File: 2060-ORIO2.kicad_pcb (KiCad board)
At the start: 4 copper layers, 99 x 99 mm, 159 parts, among them J1 TBL001-500-02GY-2GY, J101 RaspberryPI-B+header, J133 Conn_02x05_Odd_Even, J134 Conn_01x04, J301 Conn_01x08, J302 Conn_01x08, J303 Conn_01x08, J304 Conn_01x08, J305 Conn_01x08, J306 Conn_01x08, J307 Conn_01x08, J308 Conn_01x08, J321 Conn_01x08, J322 Conn_01x08, J323 Conn_01x08, J331 Conn_01x08, J332 Conn_01x08, J333 Conn_01x08, J341 Conn_01x10, J342 Conn_01x10, J343 Conn_01x10, J35 Conn_01x02, J351 Conn_01x10, J352 Conn_01x10, J353 Conn_01x10, J354 Conn_01x10, Q101 DMG2305UX-13, Q102 ULN2803ADWR, Q103 DMMT5401, SW101 SW_DIP_x08, U1 TPS563231, U10 SN74LVC4245AN, U102 AZ1117CH-3.3TRG1, U103 AZ1117CH-1.2, U104 ICE40HX4K-TQ144, U105 MCP3008, U11 AZ1117CH-3.3TRG1, U12 AP3012, U2 TPS563231, U3 SN74LVC4245AN, U4 SN74LVC4245AN, U5 SN74LVC4245AN, U6 SN74LVC4245AN, U7 SN74LVC4245AN, U8 TPS563231, U9 SN74LVC4245AN, Y101 XLH536025_000000I

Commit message: checkpoint
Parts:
- removed J133: Conn_02x05_Odd_Even, Connector_PinHeader_2.54mm:PinHeader_2x05_P2.54mm_Vertical
- removed Q101: DMG2305UX-13, digikey-footprints:SOT-23-3
- removed Q103: DMMT5401, Package_TO_SOT_SMD:SOT-23-6
- removed R101, R102: 22, Resistor_SMD:R_0603_1608Metric_Pad1.05x0.95mm_HandSolder
- removed RN102, RN103: R_Pack08, Resistor_SMD:R_Array_Convex_8x0602
- added C3: X, Capacitor_SMD:C_0603_1608Metric_Pad1.05x0.95mm_HandSolder, F.Cu at (127.1, 126.5)
- added C39: X, Capacitor_SMD:C_0603_1608Metric_Pad1.05x0.95mm_HandSolder, F.Cu at (129.6, 126.5)
- added C40: X, Capacitor_SMD:C_0603_1608Metric_Pad1.05x0.95mm_HandSolder, F.Cu at (132.2, 126.5)
- added C41: X, Capacitor_SMD:C_0603_1608Metric_Pad1.05x0.95mm_HandSolder, F.Cu at (134.7, 126.5)
- added C42: X, Capacitor_SMD:C_0603_1608Metric_Pad1.05x0.95mm_HandSolder, F.Cu at (137.2, 126.5)
- added C43: X, Capacitor_SMD:C_0603_1608Metric_Pad1.05x0.95mm_HandSolder, F.Cu at (139.8, 126.5)
- added C44: X, Capacitor_SMD:C_0603_1608Metric_Pad1.05x0.95mm_HandSolder, F.Cu at (142.3, 126.5)
- added C45: X, Capacitor_SMD:C_0603_1608Metric_Pad1.05x0.95mm_HandSolder, F.Cu at (144.9, 126.5)
- added R10: X, Resistor_SMD:R_0603_1608Metric_Pad1.05x0.95mm_HandSolder, F.Cu at (115.3, 51.3)
- added R11: X, Resistor_SMD:R_0603_1608Metric_Pad1.05x0.95mm_HandSolder, F.Cu at (118.4, 51.3)
- added R12: X, Resistor_SMD:R_0603_1608Metric_Pad1.05x0.95mm_HandSolder, F.Cu at (125.0, 62.3)
- added R13: X, Resistor_SMD:R_0603_1608Metric_Pad1.05x0.95mm_HandSolder, F.Cu at (116.8, 51.3)
- added R14: X, Resistor_SMD:R_0603_1608Metric_Pad1.05x0.95mm_HandSolder, F.Cu at (110.6, 51.3)
- added R15: X, Resistor_SMD:R_0603_1608Metric_Pad1.05x0.95mm_HandSolder, F.Cu at (113.6, 51.3)
- added R16: X, Resistor_SMD:R_0603_1608Metric_Pad1.05x0.95mm_HandSolder, F.Cu at (127.1, 129.9)
- added R17: X, Resistor_SMD:R_0603_1608Metric_Pad1.05x0.95mm_HandSolder, F.Cu at (129.6, 129.9)
- added R18: X, Resistor_SMD:R_0603_1608Metric_Pad1.05x0.95mm_HandSolder, F.Cu at (132.2, 129.9)
- added R19: X, Resistor_SMD:R_0603_1608Metric_Pad1.05x0.95mm_HandSolder, F.Cu at (134.7, 129.9)
- added R20: X, Resistor_SMD:R_0603_1608Metric_Pad1.05x0.95mm_HandSolder, F.Cu at (137.2, 129.9)
- added R21: X, Resistor_SMD:R_0603_1608Metric_Pad1.05x0.95mm_HandSolder, F.Cu at (139.8, 129.9)
- added R22: X, Resistor_SMD:R_0603_1608Metric_Pad1.05x0.95mm_HandSolder, F.Cu at (142.3, 129.9)
- added R23: X, Resistor_SMD:R_0603_1608Metric_Pad1.05x0.95mm_HandSolder, F.Cu at (144.9, 129.9)
- added R24: X, Resistor_SMD:R_0603_1608Metric_Pad1.05x0.95mm_HandSolder, F.Cu at (127.1, 123.2)
- added R25: X, Resistor_SMD:R_0603_1608Metric_Pad1.05x0.95mm_HandSolder, F.Cu at (129.6, 123.2)
- added R26: X, Resistor_SMD:R_0603_1608Metric_Pad1.05x0.95mm_HandSolder, F.Cu at (132.2, 123.2)
- added R27: X, Resistor_SMD:R_0603_1608Metric_Pad1.05x0.95mm_HandSolder, F.Cu at (134.7, 123.2)
- added R28: X, Resistor_SMD:R_0603_1608Metric_Pad1.05x0.95mm_HandSolder, F.Cu at (137.2, 123.2)
- added R29: X, Resistor_SMD:R_0603_1608Metric_Pad1.05x0.95mm_HandSolder, F.Cu at (139.8, 123.2)
- added R30: X, Resistor_SMD:R_0603_1608Metric_Pad1.05x0.95mm_HandSolder, F.Cu at (142.3, 123.2)
- added R31: X, Resistor_SMD:R_0603_1608Metric_Pad1.05x0.95mm_HandSolder, F.Cu at (144.9, 123.2)
- added R9: X, Resistor_SMD:R_0603_1608Metric_Pad1.05x0.95mm_HandSolder, F.Cu at (112.1, 51.3)
- J321: value Conn_01x08 -> Conn_01x09; footprint Connector_PinHeader_2.54mm:PinHeader_1x08_P2.54mm_Vertical -> Connector_PinHeader_2.54mm:PinHeader_1x09_P2.54mm_Vertical
- J341, J342, J343: value Conn_01x10 -> Conn_01x16; footprint Connector_PinHeader_2.54mm:PinHeader_1x10_P2.54mm_Vertical -> Connector_PinHeader_2.54mm:PinHeader_1x16_P2.54mm_Vertical
- U12: footprint Package_TO_SOT_SMD:SOT-23-5_HandSoldering -> Package_TO_SOT_SMD:SOT-23-5
- moved C120 47.4 mm to (142.9, 60.5), turned to 90 degrees
- moved RN101 45.0 mm to (121.7, 51.7)
- moved D0 44.6 mm to (120.9, 56.0), turned to 270 degrees
- moved D1 43.7 mm to (122.9, 56.0), turned to 270 degrees
- moved D2 43.0 mm to (124.9, 56.0), turned to 270 degrees
- moved D3 42.5 mm to (127.0, 56.0), turned to 270 degrees
- moved D7 42.4 mm to (135.1, 56.0), turned to 270 degrees
- moved D4 42.2 mm to (129.0, 56.0), turned to 270 degrees
- moved D6 42.2 mm to (133.1, 56.0), turned to 270 degrees
- moved D5 42.1 mm to (131.0, 56.0), turned to 270 degrees
- moved C119 37.0 mm to (123.4, 66.3)
- moved C111 34.1 mm to (119.8, 85.7), turned to 180 degrees
- moved SW101 28.1 mm to (104.1, 98.5), turned to 180 degrees
- moved R5 26.1 mm to (114.9, 107.2), turned to 0 degrees
- moved C29 25.6 mm to (109.5, 115.0), turned to 270 degrees
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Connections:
- net /IOT_197 renamed Net-(U104-Pad128)
- net Net-(J301-Pad6) renamed /FIO10
- net Net-(J303-Pad3) renamed /FIO5
- C22 pad 1: VCC_IO -> +3V3
- J101 pad 16: /CDONE -> /GPIO23
- J101 pad 18: /~CRESET~ -> /GPIO24
- J101 pad 19: /FPGA_MOSI -> /SPI_MOSI
- J101 pad 21: /FPGA_MISO -> /SPI_MISO
- J101 pad 23: /FPGA_SCLK -> /SPI_SCLK
- J101 pad 36: /FPGA_SSEL -> /GPIO16
- J301 pad 1: Net-(J301-Pad1) -> /FIO0
- J301 pad 2: Net-(J301-Pad2) -> /FIO2
- J301 pad 3: Net-(J301-Pad3) -> /FIO4
- J301 pad 4: Net-(J301-Pad4) -> /FIO6
- J301 pad 5: Net-(J301-Pad5) -> /FIO8
- J301 pad 7: Net-(J301-Pad7) -> /FIO12
- J301 pad 8: Net-(J301-Pad8) -> /FIO14
- J303 pad 1: Net-(J303-Pad1) -> /FIO1
- J303 pad 2: Net-(J303-Pad2) -> /FIO3
- J303 pad 4: Net-(J303-Pad4) -> /FIO7
- J303 pad 5: Net-(J303-Pad5) -> /FIO9
- J303 pad 6: Net-(J303-Pad6) -> /FIO11
- J303 pad 7: Net-(J303-Pad7) -> /FIO13
- J303 pad 8: Net-(J303-Pad8) -> /FIO15
- J321 pad 1: Net-(J321-Pad1) -> /VBATT_DIV
- J35 pad 1: VCC_IO -> Net-(J35-Pad1)
- J35 pad 2: Net-(J35-Pad2) -> GND
- J351 pad 4: /Qa3 -> /QA3
- R127 pad 1: /ADC0_11 -> /VBATT_DIV
- R130 pad 2: /ADC0_11 -> /VBATT_DIV
- R135 pad 2: /FPGA_SSEL -> /FPGA_SS
- R3 pad 2: VCC_IO -> +3V3
- R6 pad 1: Net-(J35-Pad2) -> Net-(J35-Pad1)
- RN104 pad 1: Net-(RN104-Pad1) -> /IOB_80
- RN104 pad 10: Net-(J301-Pad7) -> /FIO9
- RN104 pad 12: Net-(J301-Pad5) -> /FIO11
- RN104 pad 13: Net-(J301-Pad4) -> /FIO12
- RN104 pad 14: Net-(J301-Pad3) -> /FIO13
- RN104 pad 15: Net-(J301-Pad2) -> /FIO14
- RN104 pad 16: Net-(J301-Pad1) -> /FIO15
- RN104 pad 2: Net-(RN104-Pad2) -> /IOB_79
- RN104 pad 3: Net-(RN104-Pad3) -> /IOB_73
- RN104 pad 4: Net-(RN104-Pad4) -> /IOB_72
- RN104 pad 5: Net-(RN104-Pad5) -> /IOB_71
- RN104 pad 6: Net-(RN104-Pad6) -> /IOB_64
- RN104 pad 7: Net-(RN104-Pad7) -> /IOB_63
- RN104 pad 8: Net-(RN104-Pad8) -> /IOB_61
- RN104 pad 9: Net-(J301-Pad8) -> /FIO8
- RN105 pad 1: Net-(RN105-Pad1) -> /IOB_57
- RN105 pad 10: Net-(J303-Pad7) -> /FIO1
- RN105 pad 11: Net-(J303-Pad6) -> /FIO2
- RN105 pad 12: Net-(J303-Pad5) -> /FIO3
- RN105 pad 13: Net-(J303-Pad4) -> /FIO4
- RN105 pad 15: Net-(J303-Pad2) -> /FIO6
- RN105 pad 16: Net-(J303-Pad1) -> /FIO7
- RN105 pad 2: Net-(RN105-Pad2) -> /IOB_56
- RN105 pad 3: Net-(RN105-Pad3) -> /IOL_25B
- RN105 pad 4: Net-(RN105-Pad4) -> /IOL_25A
- RN105 pad 5: Net-(RN105-Pad5) -> /IOL_24B
- RN105 pad 6: Net-(RN105-Pad6) -> /IOL_24A
- RN105 pad 7: Net-(RN105-Pad7) -> /IOL_23B
- RN105 pad 8: Net-(RN105-Pad8) -> /IOL_23A
- RN105 pad 9: Net-(J303-Pad8) -> /FIO0
- S101 pad 1: /IOT_220 -> /PB0
- S101 pad 4: GND -> Net-(S101-Pad4)
- S102 pad 1: /IOT_219 -> /PB1
- S102 pad 4: GND -> Net-(S102-Pad4)
- SW101 pad 1: /SW7 -> /SW0
- SW101 pad 2: /SW6 -> /SW1
- SW101 pad 3: /SW5 -> /SW2
- SW101 pad 4: /SW4 -> /SW3
- SW101 pad 5: /SW3 -> /SW4
- SW101 pad 6: /SW2 -> /SW5
- SW101 pad 7: /SW1 -> /SW6
- SW101 pad 8: /SW0 -> /SW7
- U10 pad 14: Net-(U10-Pad14) -> /FPGA_DOUT7
- U10 pad 15: Net-(U10-Pad15) -> /FPGA_DOUT6
- U10 pad 16: Net-(U10-Pad16) -> /FPGA_DOUT5
- U10 pad 17: Net-(U10-Pad17) -> /FPGA_DOUT4
- U10 pad 18: Net-(U10-Pad18) -> /FPGA_DOUT3
- U10 pad 19: Net-(U10-Pad19) -> /FPGA_DOUT2
- U10 pad 20: Net-(U10-Pad20) -> /FPGA_DOUT1
- U10 pad 21: Net-(U10-Pad21) -> /FPGA_DOUT0
- U104 pad 1: /IOL_2A -> /FPGA_QB9
- U104 pad 10: /IOL_5B -> /FPGA_DOUT3
- U104 pad 101: /IOR_160 -> /FPGA_PWM6
- U104 pad 102: /IOR_161 -> /FPGA_PWM7
- U104 pad 104: /IOR_164 -> /FPGA_PWM8
- U104 pad 105: /IOR_165 -> /FPGA_PWM9
- U104 pad 106: /IOR_166 -> /FPGA_PWM10
- U104 pad 107: /IOR_167 -> /FPGA_PWM11
- U104 pad 11: /IOL_8A -> /FPGA_DOUT4
- U104 pad 110: /IOT_168 -> /FPGA_PWM12
- U104 pad 112: /IOT_169 -> /FPGA_PWM13
- U104 pad 113: /IOT_170 -> /FPGA_PWM14
- U104 pad 114: /IOT_171 -> /FPGA_PWM15
- U104 pad 115: /IOT_172 -> /ADC_CLK
- U104 pad 116: /IOT_173 -> /ADC_SO
- U104 pad 117: /IOT_174 -> /ADC_SI
- U104 pad 118: /IOT_177 -> /~ADC_CS
- U104 pad 119: /IOT_178 -> /FPGA_QA0
- U104 pad 12: /IOL_8B -> /FPGA_DOUT5
- U104 pad 120: /IOT_179 -> /FPGA_QB0
- U104 pad 121: /IOT_181 -> /FPGA_QA1
- U104 pad 122: /IOT_190 -> /FPGA_QB1
- U104 pad 124: /IOT_191 -> /FPGA_QA2
- U104 pad 125: /IOT_192 -> /FPGA_QB2
- U104 pad 129: /IOT_198 -> /FPGA_QA3
- U104 pad 130: /IOT_206 -> /FPGA_QB3
- U104 pad 134: /IOT_212 -> /FPGA_QA4
- U104 pad 135: /IOT_213 -> /FPGA_QB4
- U104 pad 136: /IOT_214 -> /FPGA_QA5
- U104 pad 137: /IOT_215 -> /FPGA_QB5
- U104 pad 138: /IOT_216 -> /FPGA_QA6
- U104 pad 139: /IOT_217 -> /FPGA_QB6
- U104 pad 141: /IOT_219 -> /FPGA_QA7
- U104 pad 142: /IOT_220 -> /FPGA_QB7
- U104 pad 143: /IOT_221 -> /FPGA_QA8
- U104 pad 144: /IOT_222 -> /FPGA_QB8
- U104 pad 15: /IOL_10A -> /FPGA_DOUT6
- U104 pad 16: /IOL_10B -> /FPGA_DOUT7
- U104 pad 17: /IOL_12A -> /FPGA_DIN0
- U104 pad 18: /IOL_12B -> /FPGA_DIN1
- U104 pad 19: /IOL_13A -> /FPGA_DIN2
- U104 pad 2: /IOL_2B -> /FPGA_QA9
- U104 pad 20: /IOL_13B -> /FPGA_DIN3
- U104 pad 21: /IOL_14A -> /FPGA_DIN4
- U104 pad 22: /IOL_14B -> /FPGA_DIN5
- U104 pad 23: /IOL_17A -> /FPGA_DIN6
- U104 pad 24: /IOL_17B -> /FPGA_DIN7
- U104 pad 3: /IOL_3A -> /PB0
- U104 pad 4: /IOL_3B -> /PB1
- U104 pad 52: /IOB_82 -> /LED_7
- U104 pad 55: /SPI_CE0 -> /LED_6
- U104 pad 56: /IOB_94 -> /LED_5
- U104 pad 60: /IOB_95 -> /LED_4
- U104 pad 61: /IOB_96 -> /LED_3
- U104 pad 62: /IOB_102 -> /LED_2
- U104 pad 63: /IOB_103 -> /LED_1
- U104 pad 64: /IOB_104 -> /LED_0
- U104 pad 67: /FPGA_MISO -> /FPGA_SDO
- U104 pad 68: /FPGA_MOSI -> /FPGA_SDI
- U104 pad 7: /IOL_4A -> /FPGA_DOUT0
- U104 pad 70: /FPGA_SCLK -> /FPGA_SCK
- U104 pad 71: /FPGA_SSEL -> /FPGA_SS
- U104 pad 73: /IOR_109 -> /FPGA_CE0
- U104 pad 74: /IOR_110 -> /SW7
- U104 pad 75: /IOR_111 -> /SW6
- U104 pad 76: /IOR_112 -> /SW5
- U104 pad 78: /IOR_114 -> /SW4
- U104 pad 79: /IOR_115 -> /SW3
- U104 pad 8: /IOL_4B -> /FPGA_DOUT1
- U104 pad 80: /IOR_116 -> /SW2
- U104 pad 81: /IOR_117 -> /SW1
- U104 pad 82: /IOR_118 -> /SW0
- U104 pad 83: /IOR_119 -> /SOL_7
- U104 pad 84: /IOR_120 -> /SOL_6
- U104 pad 85: /IOR_128 -> /SOL_5
- U104 pad 87: /IOR_136 -> /SOL_4
- U104 pad 88: /IOR_137 -> /SOL_3
- U104 pad 9: /IOL_5A -> /FPGA_DOUT2
- U104 pad 90: /IOR_138 -> /SOL_2
- U104 pad 91: /IOR_139 -> /SOL_1
- U104 pad 93: /IOR_140 -> /SOL_0
- U104 pad 94: /IOR_141 -> /FPGA_PWM0
- U104 pad 95: /IOR_144 -> /FPGA_PWM1
- U104 pad 96: /IOR_146 -> /FPGA_PWM2
- U104 pad 97: /IOR_147 -> /FPGA_PWM3
- U104 pad 98: /IOR_148 -> /FPGA_PWM4
- U104 pad 99: /IOR_152 -> /FPGA_PWM5
- U105 pad 10: Net-(U105-Pad10) -> /~ADC_CS
- U105 pad 11: Net-(U105-Pad11) -> /ADC_SI
- U105 pad 12: Net-(U105-Pad12) -> /ADC_SO
- U105 pad 13: Net-(U105-Pad13) -> /ADC_CLK
- U105 pad 16: VCC_IO -> +3V3
- U3 pad 10: Net-(U3-Pad10) -> /QB9
- U3 pad 14: Net-(U3-Pad14) -> /FPGA_QB9
- U3 pad 15: Net-(U3-Pad15) -> /FPGA_QA9
- U3 pad 16: Net-(U3-Pad16) -> /FPGA_QB8
- U3 pad 17: Net-(U3-Pad17) -> /FPGA_QA8
- U3 pad 18: Net-(U3-Pad18) -> /FPGA_QB7
- U3 pad 19: Net-(U3-Pad19) -> /FPGA_QA7
- U3 pad 20: Net-(U3-Pad20) -> /FPGA_QB6
- U3 pad 21: Net-(U3-Pad21) -> /FPGA_QA6
- U3 pad 3: Net-(U3-Pad3) -> /QA6
- U3 pad 4: Net-(U3-Pad4) -> /QB6
- U3 pad 5: Net-(U3-Pad5) -> /QA7
- U3 pad 6: Net-(U3-Pad6) -> /QB7
- U3 pad 7: Net-(U3-Pad7) -> /QA8
- U3 pad 8: Net-(U3-Pad8) -> /QB8
- U3 pad 9: Net-(U3-Pad9) -> /QA9
- U4 pad 10: Net-(U4-Pad10) -> /QB5
- U4 pad 14: Net-(U4-Pad14) -> /FPGA_QB5
- U4 pad 15: Net-(U4-Pad15) -> /FPGA_QA5
- U4 pad 16: Net-(U4-Pad16) -> /FPGA_QB4
- U4 pad 17: Net-(U4-Pad17) -> /FPGA_QA4
- U4 pad 18: Net-(U4-Pad18) -> /FPGA_QB3
- U4 pad 19: Net-(U4-Pad19) -> /FPGA_QA3
- U4 pad 20: Net-(U4-Pad20) -> /FPGA_QB2
- U4 pad 21: Net-(U4-Pad21) -> /FPGA_QA2
- U4 pad 3: Net-(U4-Pad3) -> /QA2
- U4 pad 4: Net-(U4-Pad4) -> /QB2
- U4 pad 5: Net-(U4-Pad5) -> /QA3
- U4 pad 6: Net-(U4-Pad6) -> /QB3
- U4 pad 7: Net-(U4-Pad7) -> /QA4
- U4 pad 8: Net-(U4-Pad8) -> /QB4
- U4 pad 9: Net-(U4-Pad9) -> /QA5
- U5 pad 10: Net-(U5-Pad10) -> /QB1
- U5 pad 14: Net-(U5-Pad14) -> /FPGA_QB1
- U5 pad 15: Net-(U5-Pad15) -> /FPGA_QA1
- U5 pad 16: Net-(U5-Pad16) -> /FPGA_QB0
- U5 pad 17: Net-(U5-Pad17) -> /FPGA_QA0
- U5 pad 7: Net-(U5-Pad7) -> /QA0
- U5 pad 8: Net-(U5-Pad8) -> /QB0
- U5 pad 9: Net-(U5-Pad9) -> /QA1
- U6 pad 10: Net-(U6-Pad10) -> /PWM15
- U6 pad 14: Net-(U6-Pad14) -> /FPGA_PWM15
- U6 pad 15: Net-(U6-Pad15) -> /FPGA_PWM14
- U6 pad 16: Net-(U6-Pad16) -> /FPGA_PWM13
- U6 pad 17: Net-(U6-Pad17) -> /FPGA_PWM12
- U6 pad 18: Net-(U6-Pad18) -> /FPGA_PWM11
- U6 pad 19: Net-(U6-Pad19) -> /FPGA_PWM10
- U6 pad 5: Net-(U6-Pad5) -> /PWM10
- U6 pad 6: Net-(U6-Pad6) -> /PWM11
- U6 pad 7: Net-(U6-Pad7) -> /PWM12
- U6 pad 8: Net-(U6-Pad8) -> /PWM13
- U6 pad 9: Net-(U6-Pad9) -> /PWM14
- U9 pad 14: Net-(U9-Pad14) -> /FPGA_DIN7
- U9 pad 15: Net-(U9-Pad15) -> /FPGA_DIN6
- U9 pad 16: Net-(U9-Pad16) -> /FPGA_DIN5
- U9 pad 17: Net-(U9-Pad17) -> /FPGA_DIN4
- U9 pad 18: Net-(U9-Pad18) -> /FPGA_DIN3
- U9 pad 19: Net-(U9-Pad19) -> /FPGA_DIN2
- U9 pad 20: Net-(U9-Pad20) -> /FPGA_DIN1
- U9 pad 21: Net-(U9-Pad21) -> /FPGA_DIN0
- Y101 pad 3: /IOB_82 -> /IOB_81
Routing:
- net +3V3: track 0.00 -> 356.2 mm, vias 0 -> 22
- net VCC_IO: track 0.00 -> 267.4 mm
- net +1V2: track 0.00 -> 144.3 mm, vias 0 -> 11
- net VCC_IO_3.3: track 0.00 -> 131.6 mm, vias 0 -> 3
- net GND: track 0.00 -> 125.3 mm, vias 0 -> 138
- net (no net): track 119.8 -> 0.00 mm
- net +BATT: track 0.00 -> 118.2 mm, vias 0 -> 3
- net /PB1: track 0.00 -> 61.3 mm, vias 0 -> 2
- net /FPGA_PWM0: track 0.00 -> 57.6 mm
- net /FPGA_PWM1: track 0.00 -> 56.4 mm
- net /FPGA_PWM2: track 0.00 -> 55.6 mm
- net /FPGA_PWM3: track 0.00 -> 55.2 mm
- net /PB0: track 0.00 -> 54.1 mm, vias 0 -> 2
- net /FPGA_PWM4: track 0.00 -> 54.1 mm
- net /FPGA_PWM5: track 0.00 -> 53.3 mm
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- removed copper zone on In1.Cu, net GND
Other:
- board size 99 x 99 mm -> 100 x 100 mm
- copper layers 4 -> 2
- net class Default: clearance 0.1524 -> 0.2032; trace_width 0.1524 -> 0.2032
- rule trace_clearance: 0.1524 -> 0.2032
- board text added: "+5"
- board text added: "10"
- board text added: "11"
- board text added: "12"
- board text added: "13"
- board text added: "14"
- board text added: "15"
- board text added: "24V"
- board text added: "3"
- board text added: "4"
- board text added: "AIN"
- board text added: "CL"
- board text added: "DA"
- board text added: "FPGA GPIO 3.3V ONLY!!"
- board text added: "I2C"
- board text added: "IN"
- board text added: "IN = 5V OUT = 3.3V"
- board text added: "OUT"
- board text added: "S"
- board text added: "SOLENOID"
- board text added: "SW"
- board text added: "VB REF"
- board text added: "⏚"
- board text removed: "3.3"
- board text removed: "FPGA IO 3.3V ONLY!!"
- board text removed: "GND"
- board text removed: "I"
- board text removed: "IN = 3.3V OUT = 5V"
- board text removed: "MISO"
- board text removed: "MOSI"
- board text removed: "O"
- board text removed: "SCK"
- board text removed: "SPI"
- board text removed: "SSEL0"
- board text removed: "SSEL1"
- board text removed: "SSEL2"
- board text removed: "SSEL3"
- board text removed: "VIO"

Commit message: Dev checkpoint (first version passing DRC)
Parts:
- added D8: DB2460600L, Diode_SMD:D_SOD-128, F.Cu at (75.8, 83.3)
- L3: footprint Inductor_SMD:L_Bourns_SRN6045TA -> Inductor_SMD:L_Taiyo-Yuden_NR-40xx_HandSoldering
- U1, U2, U8: footprint Package_TO_SOT_SMD:SOT-563 -> jb-footprint:SOT-563
- moved LOGO101 42.2 mm to (143.4, 105.1)
- moved R2 9.55 mm to (86.2, 122.9), turned to 270 degrees
- moved R1 9.45 mm to (87.7, 122.9), turned to 90 degrees
- moved C14 8.59 mm to (84.6, 128.5), turned to 90 degrees
- moved C11 8.15 mm to (80.7, 118.1), turned to 90 degrees
- moved C30 8.09 mm to (119.4, 124.0), turned to 270 degrees
- moved C12 7.21 mm to (82.9, 128.3), turned to 90 degrees
- moved C31 6.96 mm to (117.5, 124.0), turned to 270 degrees
- moved C32 6.75 mm to (115.7, 124.0), turned to 270 degrees
- moved C10 6.60 mm to (82.5, 118.3), turned to 90 degrees
- moved C13 6.55 mm to (80.9, 128.3), turned to 90 degrees
- moved C9 6.17 mm to (84.7, 122.9), turned to 270 degrees
- moved L1 5.75 mm to (76.7, 125.1), turned to 270 degrees
- moved C27 5.68 mm to (120.2, 113.4), turned to 270 degrees
- moved U8 3.53 mm to (116.7, 113.7)
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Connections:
- J101 pad 2: /PI_5 -> 5V_PI
- J101 pad 4: /PI_5 -> 5V_PI
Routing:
- net VCC_IO: track 267.4 -> 346.8 mm
- net +BATT: track 118.2 -> 182.1 mm, vias 3 -> 21
- net VCC_SOL: track 13.7 -> 46.9 mm
- net 5V_PI: track 39.8 -> 66.9 mm, vias 6 -> 13
- net VCC_PWM: track 38.1 -> 64.6 mm
- net Net-(C4-Pad2): track 0.00 -> 13.1 mm, vias 0 -> 2
- net Net-(C9-Pad2): track 0.00 -> 12.9 mm, vias 0 -> 2
- net Net-(D8-Pad2): track 0.00 -> 9.81 mm
- net GND: track 125.3 -> 133.6 mm, vias 138 -> 247
- net Net-(R1-Pad2): track 0.00 -> 7.08 mm
- net Net-(C27-Pad2): track 0.00 -> 6.62 mm
- net Net-(R107-Pad2): track 0.00 -> 6.05 mm
- net Net-(R4-Pad2): track 0.00 -> 5.91 mm
- net Net-(R7-Pad2): track 0.00 -> 4.75 mm
- net Net-(C27-Pad1): track 0.00 -> 3.94 mm
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- added copper zone on B.Cu, net +BATT
- added copper zone on F.Cu, net +BATT
- added copper zone on B.Cu, net 5V_PI
- added copper zone on F.Cu, net 5V_PI
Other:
- net class Default: clearance 0.2032 -> 0.1524
- rule trace_clearance: 0.2032 -> 0.1524
- board text added: "Rev 0.0"
- board text added: "VCCIO IN = 5V OUT = 3.3V"
- board text removed: "IN = 5V OUT = 3.3V"
- board text removed: "ORIO2 Rev 0.0"
- board text removed: "SW"

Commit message: Part value & BOM cleanup.
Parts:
- C3, C39, C40, C41, C42, C43, C44, C45: value X -> .1uF
- L1, L102, L2: value 2.2uH -> 4.7uH
- R1: value K -> 90K
- R16, R17, R18, R19, R20, R21, R22, R23, R24, R25, R26, R27, R28, R29, R30, R31: value X -> 5K
- R4: value 73K2 -> 45K3
- R6: value K -> 16K2
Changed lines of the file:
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@@
       (effects (font (size 1 1) (thickness 0.15)))
     )
-    (fp_text value X (at 0 1.43 90) (layer F.Fab)
+    (fp_text value 5K (at 0 1.43 90) (layer F.Fab)
       (effects (font (size 1 1) (thickness 0.15)))
     )
@@
       (effects (font (size 1 1) (thickness 0.15)))
     )
-    (fp_text value X (at 0 1.43 90) (layer F.Fab)
+    (fp_text value 5K (at 0 1.43 90) (layer F.Fab)
       (effects (font (size 1 1) (thickness 0.15)))
     )
@@
       (effects (font (size 1 1) (thickness 0.15)))
     )
-    (fp_text value X (at 0 1.43 90) (layer F.Fab)
+    (fp_text value 5K (at 0 1.43 90) (layer F.Fab)
       (effects (font (size 1 1) (thickness 0.15)))
     )
@@
       (effects (font (size 1 1) (thickness 0.15)))
     )
-    (fp_text value X (at 0 1.43 90) (layer F.Fab)
+    (fp_text value 5K (at 0 1.43 90) (layer F.Fab)
       (effects (font (size 1 1) (thickness 0.15)))
     )
@@
       (effects (font (size 1 1) (thickness 0.15)))
     )
-    (fp_text value X (at 0 1.43 90) (layer F.Fab)
+    (fp_text value 5K (at 0 1.43 90) (layer F.Fab)
       (effects (font (size 1 1) (thickness 0.15)))
     )
@@
       (effects (font (size 1 1) (thickness 0.15)))
     )
-    (fp_text value X (at 0 1.43 90) (layer F.Fab)
+    (fp_text value 5K (at 0 1.43 90) (layer F.Fab)
       (effects (font (size 1 1) (thickness 0.15)))
     )
@@
       (effects (font (size 1 1) (thickness 0.15)))
     )
-    (fp_text value X (at 0 1.43 90) (layer F.Fab)
+    (fp_text value 5K (at 0 1.43 90) (layer F.Fab)
       (effects (font (size 1 1) (thickness 0.15)))
     )
@@
       (effects (font (size 1 1) (thickness 0.15)))
     )
-    (fp_text value X (at 0 1.43 90) (layer F.Fab)
+    (fp_text value 5K (at 0 1.43 90) (layer F.Fab)
       (effects (font (size 1 1) (thickness 0.15)))
     )
@@
       (effects (font (size 1 1) (thickness 0.15)))
     )
-    (fp_text value X (at 0 1.43 90) (layer F.Fab)
+    (fp_text value 5K (at 0 1.43 90) (layer F.Fab)
       (effects (font (size 1 1) (thickness 0.15)))
     )
@@
       (effects (font (size 1 1) (thickness 0.15)))
     )
-    (fp_text value X (at 0 1.43 90) (layer F.Fab)
+    (fp_text value 5K (at 0 1.43 90) (layer F.Fab)
       (effects (font (size 1 1) (thickness 0.15)))
     )
@@
       (effects (font (size 1 1) (thickness 0.15)))
     )
-    (fp_text value X (at 0 1.43 90) (layer F.Fab)
+    (fp_text value 5K (at 0 1.43 90) (layer F.Fab)
       (effects (font (size 1 1) (thickness 0.15)))
     )
@@
       (effects (font (size 1 1) (thickness 0.15)))
     )
-    (fp_text value X (at 0 1.43 90) (layer F.Fab)
+    (fp_text value 5K (at 0 1.43 90) (layer F.Fab)
       (effects (font (size 1 1) (thickness 0.15)))
     )
@@
       (effects (font (size 1 1) (thickness 0.15)))
     )
-    (fp_text value X (at 0 1.43 90) (layer F.Fab)
+    (fp_text value 5K (at 0 1.43 90) (layer F.Fab)
       (effects (font (size 1 1) (thickness 0.15)))
     )
@@
       (effects (font (size 1 1) (thickness 0.15)))
     )
-    (fp_text value X (at 0 1.43 90) (layer F.Fab)
+    (fp_text value 5K (at 0 1.43 90) (layer F.Fab)
       (effects (font (size 1 1) (thickness 0.15)))
     )
@@
       (effects (font (size 1 1) (thickness 0.15)))
     )
-    (fp_text value X (at 0 1.43 90) (layer F.Fab)
+    (fp_text value 5K (at 0 1.43 90) (layer F.Fab)
       (effects (font (size 1 1) (thickness 0.15)))
     )
@@
       (effects (font (size 1 1) (thickness 0.15)))
     )
-    (fp_text value X (at 0 1.43 90) (layer F.Fab)
+    (fp_text value 5K (at 0 1.43 90) (layer F.Fab)
       (effects (font (size 1 1) (thickness 0.15)))
     )
@@
       (effects (font (size 1 1) (thickness 0.15)))
     )
-    (fp_text value X (at 0 1.43 90) (layer F.Fab)
+    (fp_text value .1uF (at 0 1.43 90) (layer F.Fab)
       (effects (font (size 1 1) (thickness 0.15)))
     )
@@
       (effects (font (size 1 1) (thickness 0.15)))
     )
-    (fp_text value X (at 0 1.43 90) (layer F.Fab)
+    (fp_text value .1uF (at 0 1.43 90) (layer F.Fab)
       (effects (font (size 1 1) (thickness 0.15)))
     )
@@
       (effects (font (size 1 1) (thickness 0.15)))
     )
-    (fp_text value X (at 0 1.43 90) (layer F.Fab)
+    (fp_text value .1uF (at 0 1.43 90) (layer F.Fab)
       (effects (font (size 1 1) (thickness 0.15)))
     )
@@
       (effects (font (size 1 1) (thickness 0.15)))
     )
-    (fp_text value X (at 0 1.43 90) (layer F.Fab)
+    (fp_text value .1uF (at 0 1.43 90) (layer F.Fab)
       (effects (font (size 1 1) (thickness 0.15)))
     )
@@
       (effects (font (size 1 1) (thickness 0.15)))
     )
-    (fp_text value X (at 0 1.43 90) (layer F.Fab)
+    (fp_text value .1uF (at 0 1.43 90) (layer F.Fab)
       (effects (font (size 1 1) (thickness 0.15)))
     )
@@
       (effects (font (size 1 1) (thickness 0.15)))
     )
-    (fp_text value X (at 0 1.43 90) (layer F.Fab)
+    (fp_text value .1uF (at 0 1.43 90) (layer F.Fab)
       (effects (font (size 1 1) (thickness 0.15)))
     )
@@
       (effects (font (size 1 1) (thickness 0.15)))
     )
-    (fp_text value X (at 0 1.43 90) (layer F.Fab)
+    (fp_text value .1uF (at 0 1.43 90) (layer F.Fab)
       (effects (font (size 1 1) (thickness 0.15)))
     )
@@
       (effects (font (size 1 1) (thickness 0.15)))
     )
-    (fp_text value X (at 0 1.43 90) (layer F.Fab)
+    (fp_text value .1uF (at 0 1.43 90) (layer F.Fab)
       (effects (font (size 1 1) (thickness 0.15)))
     )
@@
       (effects (font (size 1 1) (thickness 0.15)))
     )
-    (fp_text value K (at 0 1.43) (layer F.Fab)
+    (fp_text value 16K2 (at 0 1.43) (layer F.Fab)
       (effects (font (size 1 1) (thickness 0.15)))
     )
@@
       (effects (font (size 1 1) (thickness 0.15)))
     )
-    (fp_text value 73K2 (at 0 1.43) (layer F.Fab)
+    (fp_text value 45K3 (at 0 1.43) (layer F.Fab)
       (effects (font (size 1 1) (thickness 0.15)))
     )
@@
       (effects (font (size 1 1) (thickness 0.15)))
     )
-    (fp_text value 2.2uH (at 0 4.2 90) (layer F.Fab)
+    (fp_text value 4.7uH (at 0 4.2 90) (layer F.Fab)
       (effects (font (size 1 1) (thickness 0.15)))
     )
@@
       (effects (font (size 1 1) (thickness 0.15)))
     )
-    (fp_text value K (at 0 1.43 90) (layer F.Fab)
+    (fp_text value 90K (at 0 1.43 90) (layer F.Fab)
       (effects (font (size 1 1) (thickness 0.15)))
     )
@@
       (effects (font (size 1 1) (thickness 0.15)))
     )
-    (fp_text value 2.2uH (at 0 4.2 90) (layer F.Fab)
+    (fp_text value 4.7uH (at 0 4.2 90) (layer F.Fab)
       (effects (font (size 1 1) (thickness 0.15)))
     )
@@
       (effects (font (size 1 1) (thickness 0.15)))
     )
-    (fp_text value 2.2uH (at 0 4.2 90) (layer F.Fab)
+    (fp_text value 4.7uH (at 0 4.2 90) (layer F.Fab)
       (effects (font (size 1 1) (thickness 0.15)))
     )

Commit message: Checkpoint before re-annotate.
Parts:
- moved C1 1.55 mm to (84.3, 88.2)
- moved C2 1.55 mm to (77.5, 87.0)
- moved D8 1.55 mm to (77.3, 83.0)
- moved L3 1.55 mm to (83.3, 83.1)
- moved R7 1.55 mm to (76.6, 89.4)
- moved R8 1.55 mm to (78.1, 89.4)
- moved U12 1.55 mm to (81.7, 88.2)
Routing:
- net +BATT: track 182.1 -> 173.9 mm
- net VCC_SOL: track 46.9 -> 46.1 mm
- net GND: vias 247 -> 292

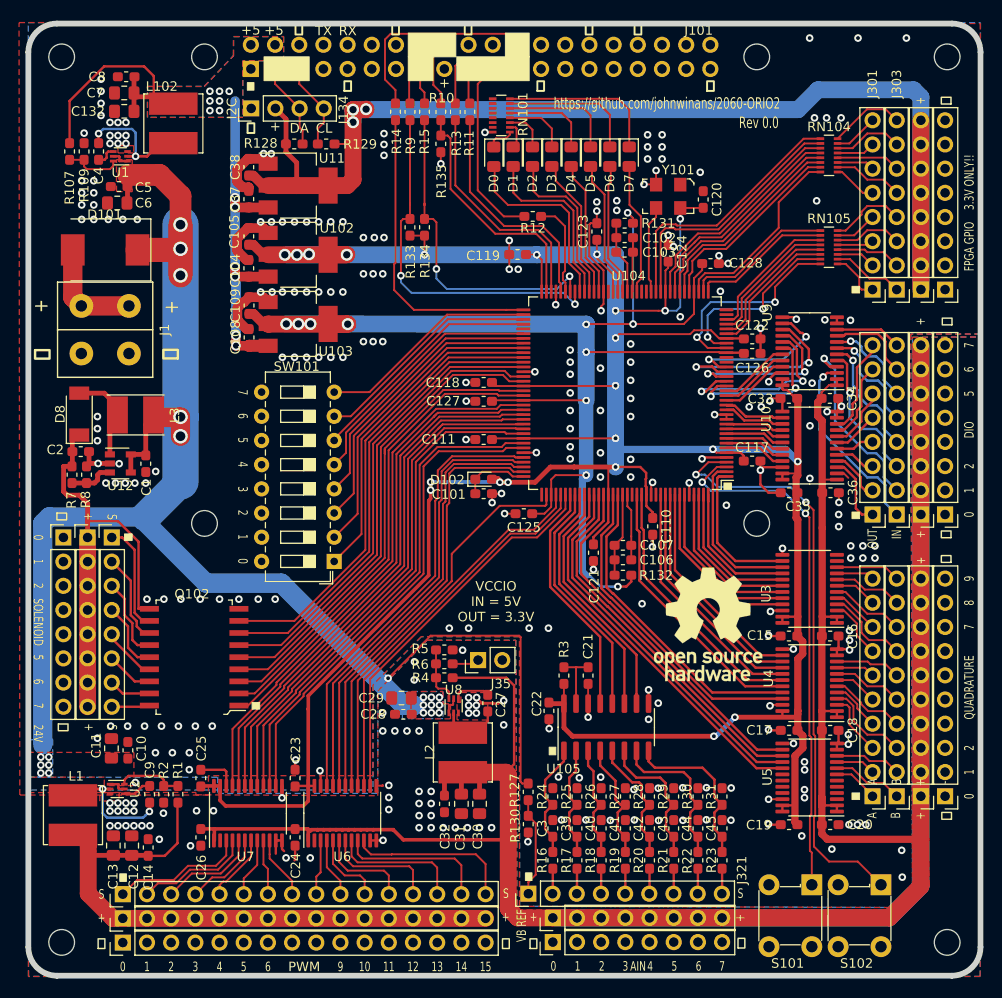
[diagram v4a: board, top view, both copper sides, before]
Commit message: Re-annotate schematic, clean silks, add NT1.
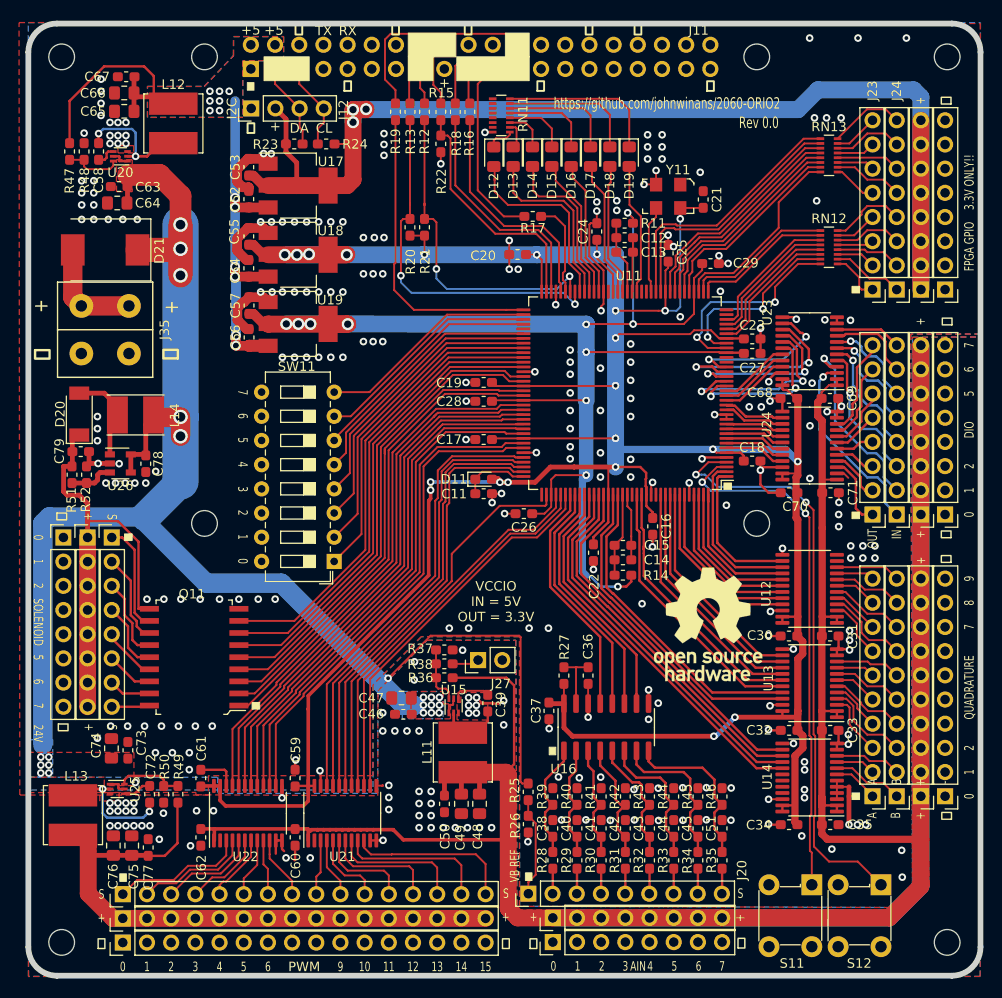
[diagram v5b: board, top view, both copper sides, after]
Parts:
- removed R131: 100, Resistor_SMD:R_0603_1608Metric_Pad1.05x0.95mm_HandSolder
- added NT1: Net-Tie_2, NetTie:NetTie-2_SMD_Pad0.5mm, F.Cu at (158.2, 122.7)
- added R11: 100, Resistor_SMD:R_0603_1608Metric_Pad1.05x0.95mm_HandSolder, F.Cu at (134.6, 63.0)
- R12: renamed from R15; value X -> 33
- R13: renamed from R9; value X -> 33
- R15: renamed from R10; value X -> 33
- R16: renamed from R11; value X -> 33
- R17: renamed from R12; value X -> 33
- R18: renamed from R13; value X -> 33
- R19: renamed from R14; value X -> 33
- R27: renamed from R3; value K -> 2K2
- R28: renamed from R16; value 5K -> 4K7
- R29: renamed from R17; value 5K -> 4K7
- R30: renamed from R18; value 5K -> 4K7
- R31: renamed from R19; value 5K -> 4K7
- R32: renamed from R20; value 5K -> 4K7
- R33: renamed from R21; value 5K -> 4K7
- R34: renamed from R22; value 5K -> 4K7
- R35: renamed from R23; value 5K -> 4K7
- R39: renamed from R24; value 5K -> 4K7
- R40: renamed from R25; value 5K -> 4K7
- R41: renamed from R26; value 5K -> 4K7
- R42: renamed from R27; value 5K -> 4K7
- R43: renamed from R28; value 5K -> 4K7
- R44: renamed from R29; value 5K -> 4K7
- R45: renamed from R30; value 5K -> 4K7
- R46: renamed from R31; value 5K -> 4K7
- RN11: renamed from RN101; value R_Pack08 -> 330
- RN12: renamed from RN105; value R_Pack08 -> 330
- RN13: renamed from RN104; value R_Pack08 -> 330
- renumbered C101 to C11, C102 to C12, C103 to C13, C106 to C14, C107 to C15, C110 to C16, C111 to C17, C117 to C18, C118 to C19, C119 to C20, C120 to C21, C121 to C22, C122 to C23, C123 to C24, C124 to C25, C125 to C26, C126 to C27, C127 to C28, C128 to C29, C15 to C30, C16 to C31, C17 to C32, C18 to C33, C19 to C34, C20 to C35, C21 to C36, C22 to C37, C3 to C38, C27 to C39, C39 to C40, C40 to C41, C41 to C42, C42 to C43, C43 to C44, C44 to C45, C28 to C46, C29 to C47, C30 to C48, C31 to C49, C32 to C50, C45 to C51, C37 to C52, C38 to C53, C104 to C54, C105 to C55, C108 to C56, C109 to C57, C4 to C58, C23 to C59, C24 to C60, C25 to C61, C26 to C62, C5 to C63, C6 to C64, C132 to C65, C7 to C66, C8 to C67, C33 to C68, C34 to C69, C35 to C70, C36 to C71, C9 to C72, C10 to C73, C11 to C74, C12 to C75, C13 to C76, C14 to C77, C1 to C78, C2 to C79, D102 to D11, D0 to D12, D1 to D13, D2 to D14, D3 to D15, D4 to D16, D5 to D17, D6 to D18, D7 to D19, D8 to D20, D101 to D21, H1 to H11, H5 to H12, H2 to H13, H6 to H14, H3 to H15, H7 to H16, H4 to H17, H8 to H18, J101 to J11, J134 to J12, J332 to J13, J333 to J14, J331 to J15, J351 to J16, J352 to J17, J353 to J18, J354 to J19, J321 to J20, J322 to J21, J323 to J22, J301 to J23, J303 to J24, J305 to J25, J307 to J26, J35 to J27, J341 to J28, J342 to J29, J343 to J30, J306 to J31, J308 to J32, J302 to J33, J304 to J34, J1 to J35, L2 to L11, L102 to L12, L1 to L13, L3 to L14, LOGO101 to LOGO11, Q102 to Q11, R132 to R14, R133 to R20, R134 to R21, R135 to R22, R128 to R23, R129 to R24, R127 to R25, R130 to R26, R4 to R36, R5 to R37, R6 to R38, R107 to R47, R109 to R48, R1 to R49, R2 to R50, R7 to R51, R8 to R52, S101 to S11, S102 to S12, SW101 to SW11, U104 to U11, U3 to U12, U4 to U13, U5 to U14, U8 to U15, U105 to U16, U11 to U17, U102 to U18, U103 to U19, U1 to U20, U6 to U21, U7 to U22, U9 to U23, U10 to U24, U2 to U25, U12 to U26, Y101 to Y11
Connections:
- U14 pad 3: Net-(U5-Pad3) -> Net-(NT1-Pad2)
- U14 pad 4: Net-(U5-Pad4) -> Net-(NT1-Pad2)
- U14 pad 5: Net-(U5-Pad5) -> Net-(NT1-Pad2)
- U14 pad 6: Net-(U5-Pad6) -> Net-(NT1-Pad2)
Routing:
- net Net-(NT1-Pad2): track 0.00 -> 3.22 mm
- net GND: track 133.6 -> 136.6 mm
